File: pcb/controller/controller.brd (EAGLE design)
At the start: 73.7 x 76.2 mm, 92 parts, among them J1 DL-2MM-HEADER-14, J10 SNG-100-HEADER-03-HDR-V, J2 DL-1.25MM-HEADER-20, J3 MICRO_SD, J4 SNG-2MM-HEADER-03-SMT-V, J5 7498011122R, J6 USB_A, J7 SNG-2MM-HEADER-09-V, J8 CUI-PJ-013C, J9 SNG-100-HEADER-04-HDR-V, Q1 12MHz, U1 LM3526M-L, U2 ARIA_G25, U3 PCM2704C, U4 TPA2005D1DGN, U5 ADP2303ARDZ, U6 TPS62086RLT, U7 TS4040D30IDBZ

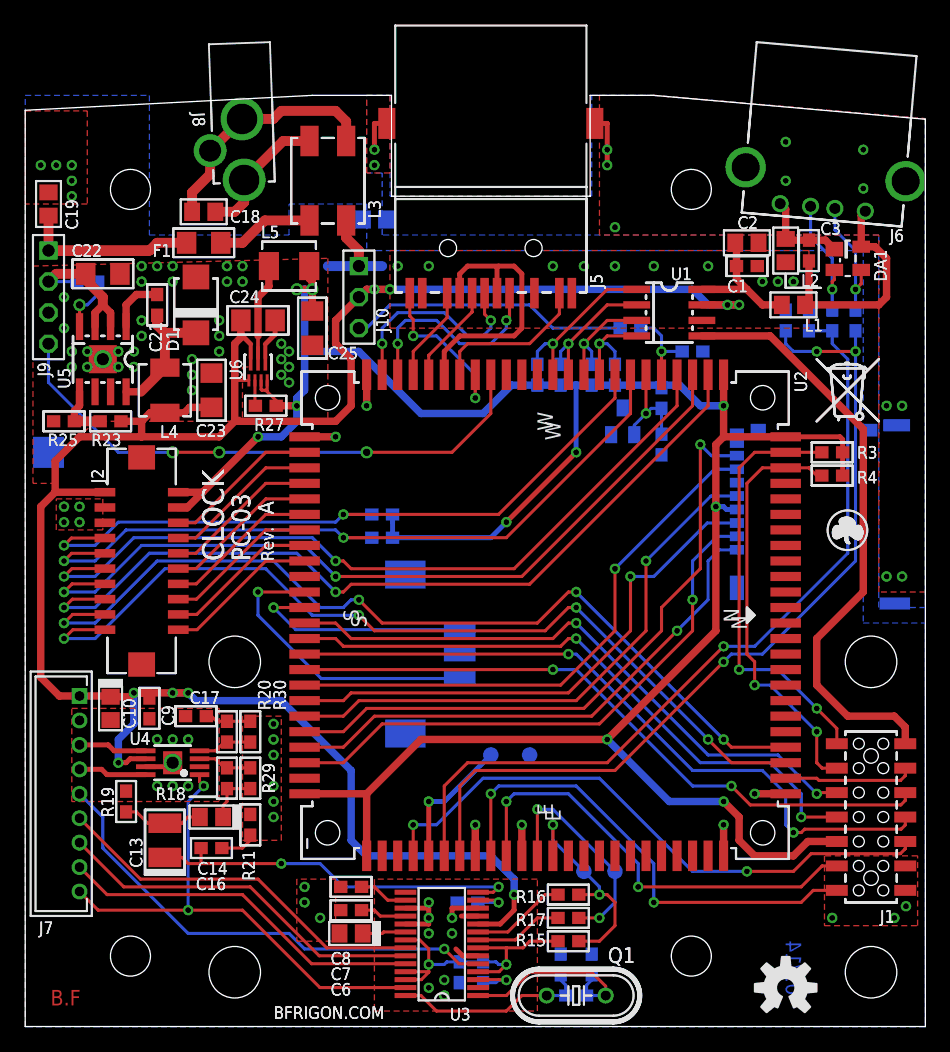
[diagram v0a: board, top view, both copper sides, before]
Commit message: Corrected drawings of touch panel PCB
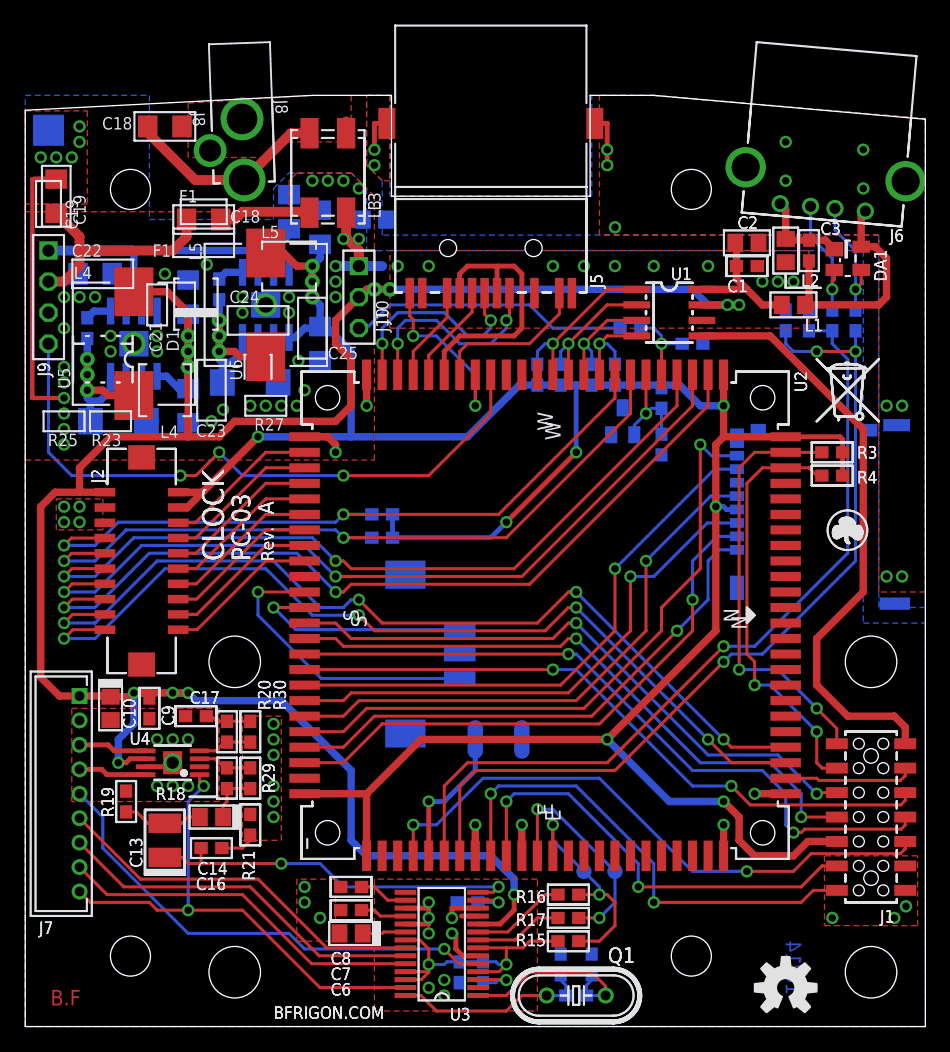
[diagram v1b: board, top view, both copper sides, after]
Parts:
- removed R22, R27: 100k, Passive:SMD_0603
- removed R23: 53.6K 1%, Passive:SMD_0603
- removed R25: 10K 1%, Passive:SMD_0603
- added C15: 10uF 10v, Passive:SMD_1206
- added C27: 22uF 6.3V, Passive:SMD_1206
- added C28: 47uF 6.3v, Passive:SMD_1206
- added D2: 30V 4A, Passive:DIODE_DO214-AA
- C13: value 100uF -> 100uF 10V
- C14: value 1uF -> 1uF 10V
- C16: value 22nF -> 0.022uF 10V
- C18, C19: value 10uF 50V -> 10uF 25V; device Passive:SMD_0805 -> Passive:SMD_1206
- C21: value 100nF -> 100nF 25v
- C22: value 10uF 50v -> 10uF 25v
- C23: value 100uF -> 22uF 6.3V
- C24: value (none) -> 100nF; device Passive:SMD_1206 -> Passive:SMD_0603
- C25: value (none) -> 47uF 6.3v
- C26: value (none) -> 100nF
- C4, C5: value (none) -> 18pF
- D1: value 40V 3A -> 30V 4A
- L4: value (none) -> 10uH; device Passive:IND_4020 -> Passive:IND-10X10
- L5: value (none) -> 4.7uH; device Passive:IND_4045 -> Passive:IND-10X10
- TP1, TP2: device Misc:TP_050 -> Misc:WIRE_SMT
- U5: value ADP2303ARDZ -> ADP2302ARDZ-5.0
- U6: value TPS62086RLT -> ADP2303ARDZ-3.3; device Power:QFN-7 -> Power:SOIC8-EP
- U7: value TS4040D30IDBZ -> LM4040D25IDBZR
- moved TP3 26.4 mm to (1.91, 73.3)
- moved D1 11.4 mm to (7.62, 49.5), flipped to the bottom, turned to 0 degrees
- moved C23 7.85 mm to (13.3, 59.7), flipped to the bottom
- moved C18 7.67 mm to (11.4, 73.7), turned to 0 degrees
- moved C21 6.02 mm to (5.08, 57.1), flipped to the bottom
- moved U6 5.12 mm to (19.7, 59.1), flipped to the bottom, turned to 180 degrees
- moved L4 4.58 mm to (8.89, 55.9), turned to 90 degrees
- moved C24 4.07 mm to (15.9, 60.3), flipped to the bottom, turned to 270 degrees
- moved L5 3.70 mm to (19.7, 59.1)
- moved U5 2.84 mm to (8.89, 55.9), flipped to the bottom
- moved F1 1.91 mm to (14.6, 66.0)
- moved TP1 1.80 mm to (36.8, 23.5), turned to 90 degrees
- moved TP2 1.42 mm to (40.6, 23.5), turned to 270 degrees
- moved C25 1.42 mm to (24.1, 55.9), flipped to the bottom
- moved C19 0.90 mm to (2.54, 67.9)
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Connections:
- net N$2 renamed IN_GND
- removed net N$3: R22.2, U5.4
- removed net N$34: R23.1, R25.2, U5.5
- removed net N$35: L5.1, U6.6
- new net N$10: C24.2, D2.K, L5.1, U6.8
- net 3.3V: now also C28.1, U6.5; no longer R27.2, U6.3, U6.4
- net 5V: now also C27.1, U5.5; no longer C24.1, R23.2, U6.1, U6.7
- net GND: now also C15.2, C27.2, C28.2, D2.A, U6.7, U6.EP; no longer C24.2, R25.1, U6.5
- net N$36: now also C24.1, U6.1; no longer R27.1, U6.2
- net VCC: now also C15.1, J9.1, U6.2, U6.3; no longer J9.2, R22.1
- net V_MAIN: now also J9.2; no longer J9.1
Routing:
- net GND: track 42.5 -> 77.4 mm, vias 86 -> 91
- net VCC: track 13.1 -> 33.3 mm
- net IN_GND: track 20.1 -> 0.97 mm
- net N$10: track 0.00 -> 16.6 mm, vias 0 -> 3
- net N$35: track 7.92 -> 0.00 mm
- net V_AUX_ON: track 46.2 -> 52.7 mm
- net N$4: track 11.2 -> 16.9 mm
- net N$33: track 11.1 -> 16.6 mm, vias 0 -> 3
- net N$34: track 4.70 -> 0.00 mm
- net N$3: track 4.67 -> 0.00 mm, vias 1 -> 0
- net V_MAIN: track 22.7 -> 18.8 mm
- net 3.3V: track 206.0 -> 209.4 mm
- net N$11: track 4.67 -> 2.13 mm
- net ETH_LINK: track 13.8 -> 15.1 mm
- net N$1: track 11.1 -> 11.8 mm
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- added copper zone on layer 1, net IN_GND
- removed copper zone on layer 1, net 5V

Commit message: Display base pcb (rev C), Touch panel (rev B)
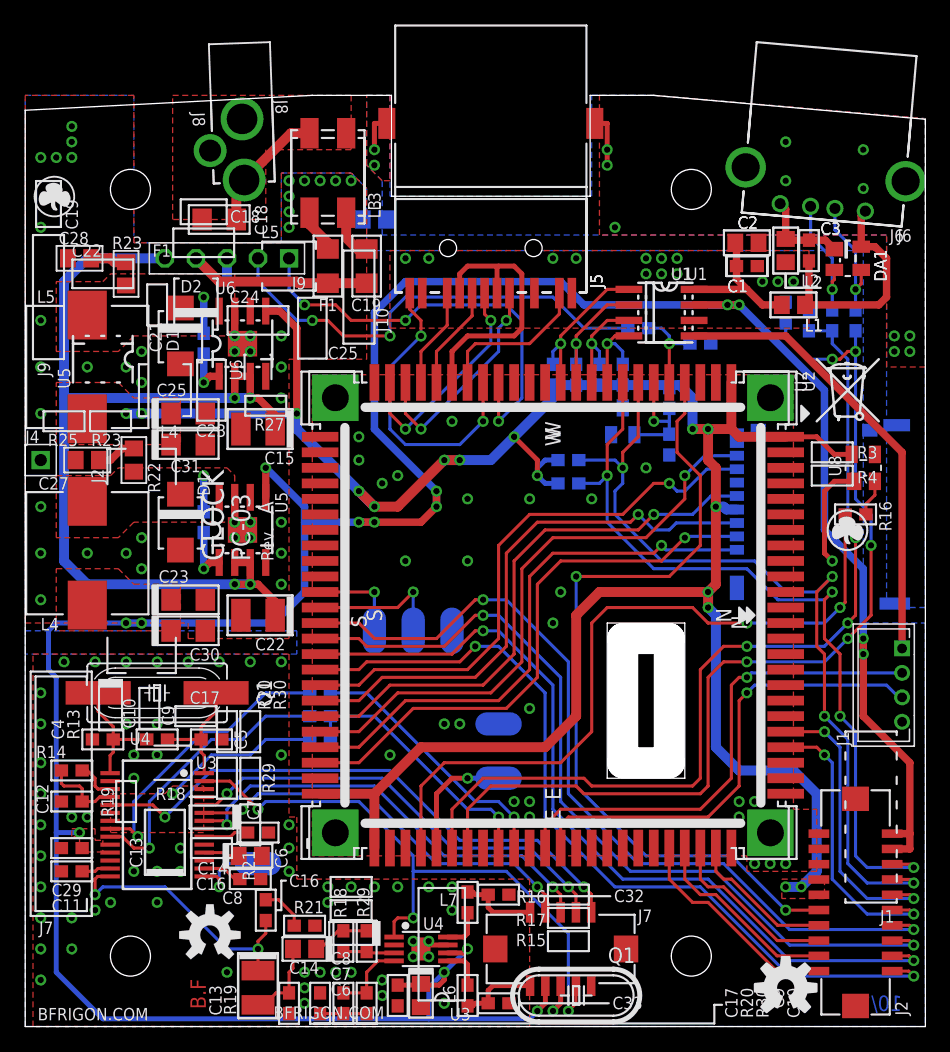
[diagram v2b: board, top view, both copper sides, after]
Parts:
- removed J10: SNG-100-HEADER-03-HDR-V, Connectors:HDR_M_3
- removed R17: 22, Passive:SMD_0603
- removed TP3: (no value), Misc:TP_75X75
- removed TP4, TP5: (no value), Misc:TP_050
- removed U$5: (no value), Symbols:TRASH_SMALL
- added C29: 1uF, Passive:SMD_0603
- added C30: 22uF (10v), Passive:CAP_S1206
- added C31: 47uF (6.3v), Passive:CAP_S1206
- added C32, C33: N/A, Passive:SMD_0603
- added L6, L7: 0, Passive:SMD_0603
- added R22, R23: 1 (1%), Passive:SMD_0805
- added U8: CAT811TTBI, IC:SOT143
- added W1: (no value), Misc:WIRE_SMT_150X75
- added W2: DRX, Misc:WIRE_SMT_150X75
- added W3: DTX, Misc:WIRE_SMT_150X75
- added W4: GND, Misc:WIRE_SMT_150X75
- C15: value 10uF 10v -> 10uF (25v); device Passive:SMD_1206 -> Passive:CAP_S1210
- C21: value 100nF 25v -> 100nF 25V
- C22: value 10uF 25v -> 10uF (25v); device Passive:SMD_1206 -> Passive:CAP_S1210
- C23: value 22uF 6.3V -> 22uF (10v); device Passive:SMD_1206 -> Passive:CAP_S1206
- C24: value 100nF -> 100nF 25V
- C25: value 47uF 6.3v -> 47uF (6.3v); device Passive:SMD_1206 -> Passive:CAP_S1206
- C27: value 22uF 6.3V -> 1nF; device Passive:SMD_1206 -> Passive:SMD_0805
- C28: value 47uF 6.3v -> 1nF; device Passive:SMD_1206 -> Passive:SMD_0805
- D1: value 30V 4A -> 30V 2A
- J1: value DL-2MM-HEADER-14 -> SNG-2MM-HEADER-04-V; device Connectors:3M-956214-2XXX -> Connectors:DF3X-4P-2DSA
- J4: value SNG-2MM-HEADER-03-SMT-V -> SNG-100-HEADER-01-HDR-V; device Connectors:DF3DZ-3P-2VXX -> Connectors:HDR_M_1
- J7: value SNG-2MM-HEADER-09-V -> DL-1.25MM-HEADER-10; device Connectors:DF3X-9P-2DSA -> Connectors:DF13A-10DP-1.25
- J9: value SNG-100-HEADER-04-HDR-V -> SNG-100-HEADER-05-HDR-V; device Connectors:HDR_M_4 -> Connectors:HDR_M_5
- L4: value 10uH -> 22uH
- L5: value 4.7uH -> 22uH
- Q1: device Crystal:HC49/S -> Crystal:HC49UP
- R1, R2: value 10k -> 22
- R16: value 22 -> 2.2k
- R21: value 16 1% -> 16 (1%)
- R24: value 12M 1% -> 12M (1%)
- R26: value 4.7M 1% -> 4.7M (1%)
- TP1, TP2: device Misc:WIRE_SMT -> Misc:WIRE_SMT_150X75
- U3: value PCM2704C -> PCM2704CDB; device IC:TSSOP28 -> IC:SSOP28
- moved U$4 70.4 mm to (2.41, 67.9)
- moved J2 64.8 mm to (67.9, 10.2)
- moved U$1 47.3 mm to (15.1, 7.49)
- moved C4 44.0 mm to (6.35, 23.5), flipped to the top, turned to 180 degrees
- moved Q1 42.3 mm to (10.8, 27.3), turned to 0 degrees
- moved J7 41.4 mm to (43.8, 6.35), turned to 0 degrees
- moved R13 40.2 mm to (10.8, 23.5), flipped to the top
- moved R16 39.0 mm to (67.9, 41.9)
- moved J4 37.8 mm to (1.27, 46.4), flipped to the top, turned to 0 degrees
- moved R14 37.5 mm to (3.81, 21.0), flipped to the top, turned to 0 degrees
- moved C12 34.7 mm to (3.81, 18.4), flipped to the top, turned to 180 degrees
- moved C10 34.6 mm to (32.4, 2.54)
- moved C5 34.0 mm to (15.2, 23.5), flipped to the top, turned to 0 degrees
- moved C11 32.5 mm to (3.81, 12.7), flipped to the top, turned to 180 degrees
- moved C9 31.1 mm to (30.5, 2.54)
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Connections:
- net N$21 renamed HID1
- net N$23 renamed VOUTL
- removed net !RESET: J1.10, U2.E21
- removed net 1WIRE: U2.S2
- removed net AD2: J2.13, U2.W22
- removed net AD3: J2.15, U2.W23
- removed net EXP_MISO: J1.6, U2.S9
- removed net EXP_MOSI: J1.8, U2.S10
- removed net EXP_NPCS0: J1.5, U2.S12
- removed net EXP_SPCK: J1.7, U2.S11
- removed net N$10: C24.2, D2.K, L5.1, U6.8
- removed net N$22: J7.8, U3.24
- removed net N$30: J7.5, U3.5
- removed net N$33: C21.2, D1.K, L4.1, U5.8
- removed net PA0: J2.6, U2.S23
- removed net PA1: J2.8, U2.S22
- removed net PA2: J2.10, U2.S21
- removed net PA23: U2.W10
- removed net PA24: U2.W11
- removed net PA25: U2.W12
- removed net PA3: J2.12, U2.S20
- removed net PA4: J2.14, U2.S19
- removed net PA5: J2.16, U2.S18
- removed net PA6: J2.18, U2.S17
- removed net PA7: J2.20, U2.S16
- removed net PA8: U2.S15
- removed net PC17: U2.N19
- removed net PWM0: U2.N20
- removed net PWM1: J2.17, U2.N21
- removed net PWM2: J2.19, U2.N22
- removed net PWM3: J1.4, U2.N23
- removed net SCL1: J1.3, R4.2, U2.N3
- removed net SDA1: J1.1, R3.2, U2.N2
- new net DOUT: J7.1, U3.5
- new net HID0: J7.5, U3.22
- new net HID2: J7.3, U3.24
- new net MISO: J2.20, U2.S9
- new net MOSI: J2.18, U2.S10
- new net N$2: C27.1, R22.1
- new net N$21: R16.1, U8.2
- new net N$3: C28.1, R23.1
- new net NRST: R16.2, U2.E21
- new net PC18/PWM0: J2.10, U2.N20
- new net PC19/PWM1: J2.12, U2.N21
- new net PC22/TXD3: J2.13, U2.E2
- new net PC23/RXD3: J2.15, U2.E3
- new net PC24/RTS3: J2.17, U2.E4
- new net PC25/CTS3: J2.19, U2.E5
- new net SPCK: J2.16, U2.S11
- new net SPI_CS0: J2.14, U2.S12
- new net SPK+: C33.1, J7.10, L6.2
- new net SPK-: C32.1, J7.9, L7.2
- new net SW_3.3: C24.2, D2.K, L5.1, R23.2, U6.8
- new net SW_5V: C21.2, D1.K, L4.1, R22.2, U5.8
- net 3.3V: now also C25.+, C31.+, J2.7, J2.9, U8.4; no longer C25.1, C28.1, J1.9, J2.2, J2.4, R1.1, R2.1
- net 5V: now also C23.+, C29.1, C30.+, J2.2, J2.4, J7.8; no longer C23.1, C27.1, J10.2, J2.1, J7.1
- net DAC_SHDN: now also J7.4; no longer J7.9
- net DRX: now also W2.1; no longer J4.1
- net DTX: now also W3.1; no longer J4.3
- net GND: now also C15.-, C22.-, C23.-, C25.-, C29.2, C30.-, C31.-, C32.2, C33.2, J1.4, J2.1, J4.1, J7.6, U2.GND@1, U2.GND@2, U2.GND@3, U2.GND@4, U8.1, W4.1; no longer C15.2, C22.2, C23.2, C25.2, J1.12, J1.14, J10.1, J4.2, J7.2, TP3.1
- net N$12: now also R2.2; no longer R16.2
- net N$13: now also R1.2; no longer R17.2
- net N$15: now also C6.+; no longer C7.1
- net N$16: now also C7.1; no longer C6.+
- net N$20: now also U3.15, W1.1; no longer J7.6, U3.22
- net N$24: now also L6.1; no longer J7.3
- net N$25: now also L7.1; no longer J7.4
- net SCL0: now also J2.8, R4.2; no longer J2.9, R2.2
- net SDA0: now also J2.6, R3.2; no longer J2.7, R1.2
- net USBB_5V: now also J1.1; no longer J1.2
- net USBB_D+: now also R15.1, R2.1; no longer J1.13
- net USBB_D-: now also R1.1; no longer J1.11
- net USBC_D+: now also J1.3; no longer R15.1, R16.1, TP4.1
- net USBC_D-: now also J1.2; no longer R17.1, TP5.1
- net VCC: now also C15.+, C22.+, J9.5; no longer C15.1, C22.1, J9.1
- net V_AUX_MON: now also J9.2; no longer J10.3
- net V_AUX_ON: now also J9.1; no longer J9.4
- net V_MAIN: now also J9.4; no longer J9.2
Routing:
- net PWM1: track 73.7 -> 0.00 mm, vias 4 -> 0
- net PWM2: track 73.2 -> 0.00 mm, vias 4 -> 0
- net SPI_CS0: track 0.00 -> 69.8 mm, vias 0 -> 2
- net SPCK: track 0.00 -> 68.9 mm, vias 0 -> 2
- net MISO: track 0.00 -> 68.4 mm, vias 0 -> 2
- net MOSI: track 0.00 -> 68.4 mm, vias 0 -> 2
- net AD3: track 68.3 -> 0.00 mm, vias 2 -> 0
- net AD2: track 66.0 -> 0.00 mm, vias 2 -> 0
- net 5V: track 185.1 -> 245.0 mm, vias 12 -> 15
- net NRST: track 0.00 -> 59.5 mm, vias 0 -> 2
- net EXP_MOSI: track 57.6 -> 0.00 mm, vias 2 -> 0
- net EXP_MISO: track 54.5 -> 0.00 mm, vias 2 -> 0
- net GND: track 77.4 -> 23.1 mm, vias 91 -> 143
- net EXP_SPCK: track 51.2 -> 0.00 mm, vias 2 -> 0
- net EXP_NPCS0: track 50.4 -> 0.00 mm, vias 2 -> 0
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- added copper zone on layer 1, net 3.3V
- added copper zone on layer 1, net 5V
- added copper zone on layer 1, net DAC_VDD
- added copper zone on layer 16, net N$10
- added copper zone on layer 1, net SW_3.3
- added copper zone on layer 1, net SW_5V
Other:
- board text added: "A-R"
- board text added: "DEBUG"

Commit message: Changed page format on schematics to US letter (8.5" x 11")
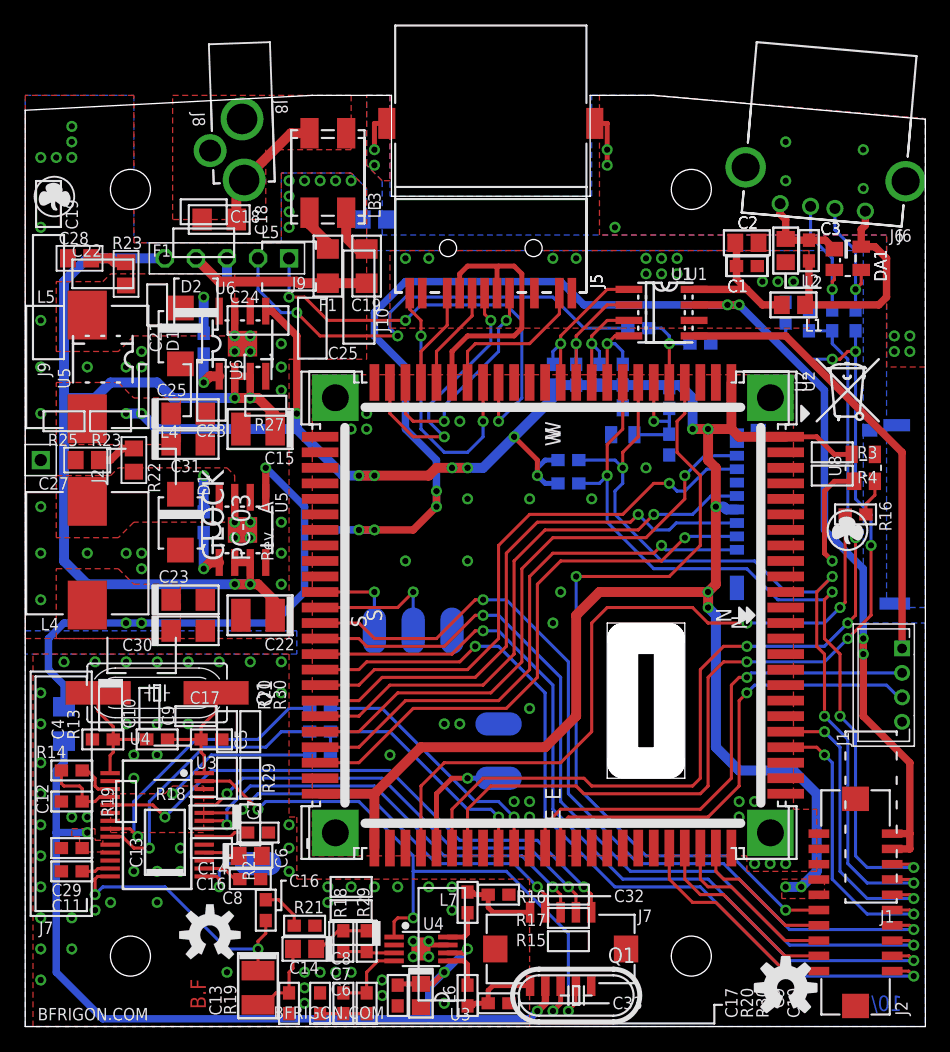
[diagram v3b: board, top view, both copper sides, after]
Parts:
- added R17: (no value), Passive:SMD_1206
- moved R1 1.27 mm to (24.1, 26.0)
- moved R15 1.27 mm to (24.1, 22.2)
- moved R2 1.27 mm to (24.1, 24.1)
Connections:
- new net 5V_AUD: C10.+, C29.1, C9.1, J7.8, R17.2, U3.10, U4.6
- net 5V: now also R17.1; no longer C10.+, C29.1, C9.1, J7.8, U3.10, U4.6
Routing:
- net 5V: track 245.0 -> 164.5 mm, vias 15 -> 11
- net 5V_AUD: track 0.00 -> 78.4 mm, vias 0 -> 4
- net ETH_RX+: track 18.6 -> 22.4 mm
- net 3.3V: track 195.8 -> 193.4 mm
- net ETH_LINK: track 24.7 -> 22.3 mm
- net VCC: track 79.8 -> 82.1 mm
- net V_AUX_MON: track 37.5 -> 38.8 mm
- net USBB_D-: track 21.8 -> 21.2 mm
- net USBB_D+: track 21.6 -> 21.1 mm
- net N$13: track 23.6 -> 23.1 mm
- net N$12: track 23.4 -> 22.9 mm
- net DAC_VDD: track 19.5 -> 19.0 mm
- added copper zone on layer 1, net 5V_AUD
